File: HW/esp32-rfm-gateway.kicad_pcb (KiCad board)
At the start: 2 copper layers, 99 x 93.5 mm, 88 parts, among them J1 ph_1x2, J2 ph_1x2, J20 220V~, J21 ph_1x2, J22 s14500, J23 s18650, J24 ph_1x3, J25 ph_1x2, J3 ph_1x3, J30 AntSMA, J4 ph_1x4, J40 ph_1x2, J5 ph_1x4, J6 ph_1x3, J7 ph_1x4, J8 ph_1x6, Q20 IRLML2244, Q40 BC817, Q41 BC817, U1 ESP-WROOM-32, U2 BD48K30, U20 IRM-05, U21 MCP73832T-2ACI, U22 BD49K35, U23 TLV62569DBV, U24 TLV379IDBV, U30 RFM9x, U40 AT_CryptoAuth, U41 HDC1080DMB

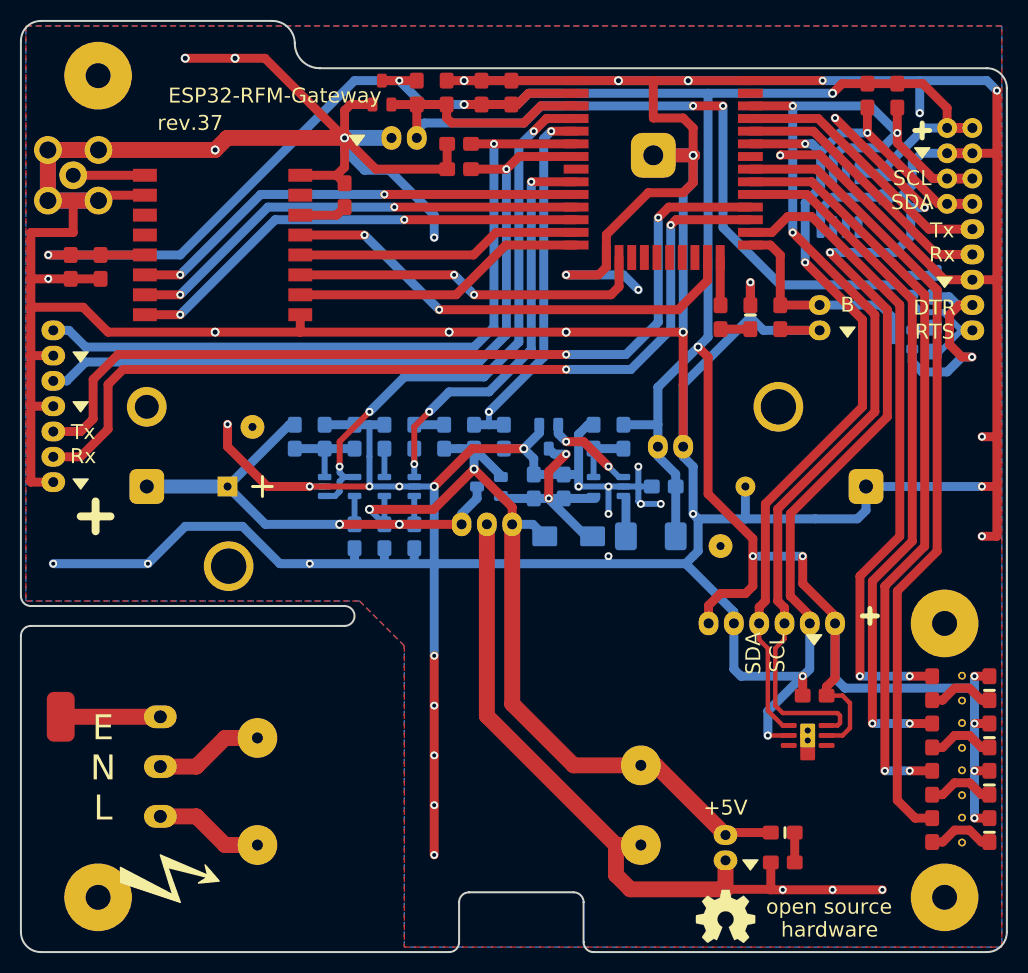
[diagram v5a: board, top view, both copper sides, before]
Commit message: Improves the labels and label positioning.
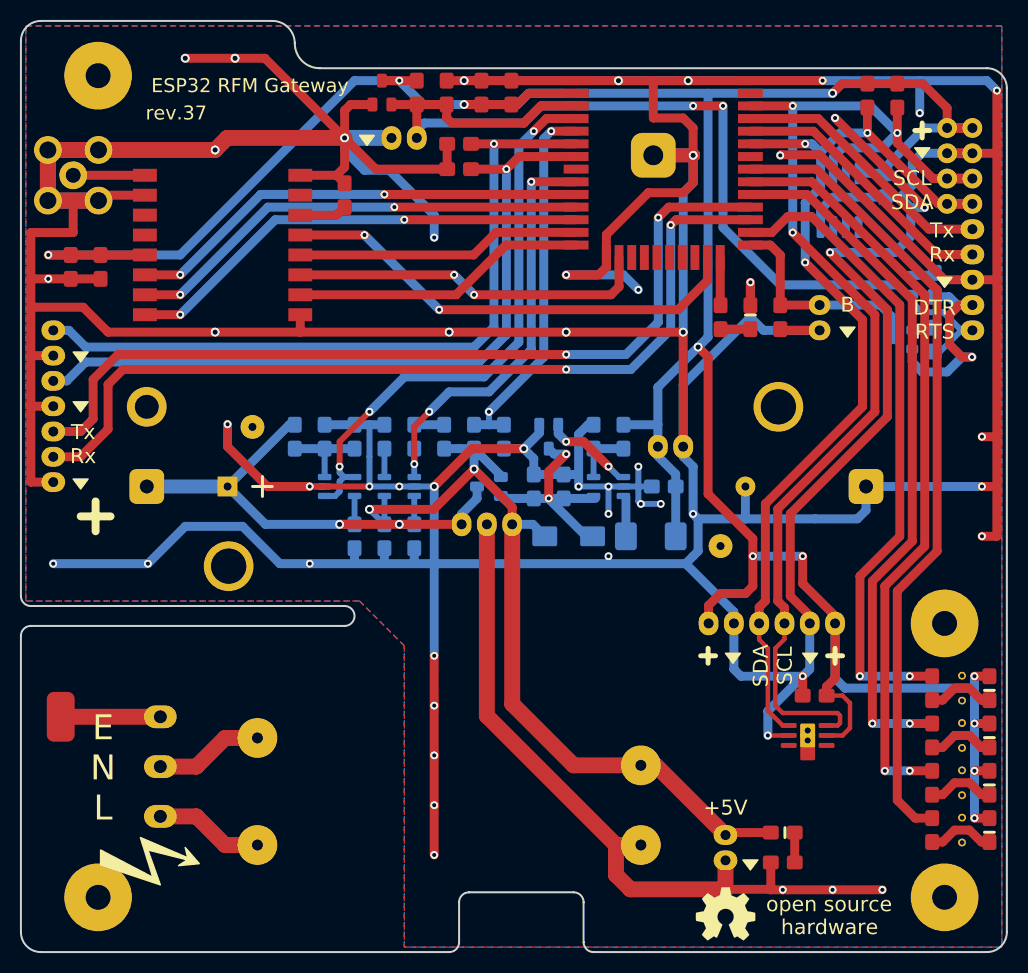
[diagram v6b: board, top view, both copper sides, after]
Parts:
- SYM5: value ESP32-RFM-Gateway -> ESP32 RFM Gateway
- moved SYM5 4.10 mm to (58.2, 53.8)
- moved SYM3 2.66 mm to (49.0, 128.2)
- moved SYM2 0.25 mm to (106.8, 133.8)
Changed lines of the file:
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@@
   (general
     (thickness 1.6)
-    (drawings 64)
+    (drawings 67)
     (tracks 745)
     (zones 0)
@@
   )
   (setup
-    (last_trace_width 0.9)
+    (last_trace_width 0.25)
     (user_trace_width 0.45)
     (user_trace_width 0.6)
@@
   )
   (module CalinGeneric:Symbol_HighVoltage_SilkS (layer F.Cu)
-    (at 51 130 90)
+    (at 49 128.25 90)
     (attr virtual)
     (fp_text reference SYM3 (at 0 -6 90) (layer F.Fab) hide
@@
   )
   (module CalinGeneric:OSHW-Logo_SilkS (layer F.Cu)
-    (at 106.75 134)
+    (at 106.75 133.75)
     (tags "Logo OSHW")
     (attr virtual)
@@
   )
   (module CalinGeneric:ValueAsText (layer F.Cu)
-    (at 61.5 51.25)
+    (at 58.25 53.75)
     (attr virtual)
     (fp_text reference SYM5 (at 0 0) (layer F.Fab) hide
       (effects (font (size 1 1) (thickness 0.15)))
     )
-    (fp_text value ESP32-RFM-Gateway (at 0 0) (layer F.SilkS)
-      (effects (font (size 1.5 1.5) (thickness 0.3)))
+    (fp_text value "ESP32 RFM Gateway" (at 0.75 -3.5) (layer F.SilkS)
+      (effects (font (size 1.4 1.4) (thickness 0.3)))
     )
     (fp_line (start -2.5 0) (end 2.5 0) (layer F.Fab) (width 0.15))
@@
       (effects (font (size 1 1) (thickness 0.15)))
     )
-    (fp_text value ph_1x6 (at 2.54 3.81) (layer F.Fab)
+    (fp_text value ph_1x6 (at -2.25 6) (layer F.Fab)
       (effects (font (size 1 1) (thickness 0.15)))
     )
@@
     )
   )
+  (gr_poly (pts (xy 106.75 107.25) (xy 108.25 107.25) (xy 107.5 108.25)) (layer F.SilkS) (width 0.15))
+  (gr_line (start 104.25 107.5) (end 105.75 107.5) (layer F.SilkS) (width 0.5))
+  (gr_line (start 105 106.75) (end 105 108.25) (layer F.SilkS) (width 0.5))
   (gr_text +5V (at 106.75 122.75) (layer F.SilkS)
     (effects (font (size 1.5 1.5) (thickness 0.3)))
   )
   (gr_poly (pts (xy 108.5 128) (xy 110 128) (xy 109.25 129)) (layer F.SilkS) (width 0.15))
-  (gr_line (start 120.5 103.5) (end 122 103.5) (layer F.SilkS) (width 0.5))
-  (gr_line (start 121.25 102.75) (end 121.25 104.25) (layer F.SilkS) (width 0.5))
-  (gr_text "SDA\nSCL" (at 110.75 107.25 90) (layer F.SilkS)
+  (gr_line (start 117 107.5) (end 118.5 107.5) (layer F.SilkS) (width 0.5))
+  (gr_line (start 117.75 106.75) (end 117.75 108.25) (layer F.SilkS) (width 0.5))
+  (gr_text "SDA\nSCL" (at 111.5 108.5 90) (layer F.SilkS)
     (effects (font (size 1.5 1.5) (thickness 0.3)))
   )
-  (gr_poly (pts (xy 114.9 105.4) (xy 116.4 105.4) (xy 115.65 106.4)) (layer F.SilkS) (width 0.15))
+  (gr_poly (pts (xy 114.5 107.25) (xy 116 107.25) (xy 115.25 108.25)) (layer F.SilkS) (width 0.15))
   (gr_line (start 126.5 54) (end 126.5 55.5) (layer F.SilkS) (width 0.5))
   (gr_line (start 125.75 54.75) (end 127.25 54.75) (layer F.SilkS) (width 0.5))
@@
   (gr_poly (pts (xy 41.25 82) (xy 42.75 82) (xy 42 83)) (layer F.SilkS) (width 0.15))
   (gr_poly (pts (xy 41.25 77) (xy 42.75 77) (xy 42 78)) (layer F.SilkS) (width 0.15))
-  (gr_poly (pts (xy 69 55.25) (xy 70.5 55.25) (xy 69.75 56.25)) (layer F.SilkS) (width 0.15))
+  (gr_poly (pts (xy 70 55.25) (xy 71.5 55.25) (xy 70.75 56.25)) (layer F.SilkS) (width 0.15))
   (gr_poly (pts (xy 118.25 74.5) (xy 119.75 74.5) (xy 119 75.5)) (layer F.SilkS) (width 0.15))
   (gr_text B (at 119 72.25) (layer F.SilkS)
     (effects (font (size 1.5 1.5) (thickness 0.3)))
   )
-  (gr_text "designed with KiCad\nfor hand soldering" (at 93.75 122.5) (layer B.SilkS)
+  (gr_text "designed with KiCad\nfor hand soldering" (at 93.5 122.5) (layer B.SilkS)
     (effects (font (size 1.5 1.5) (thickness 0.3)) (justify left mirror))
   )
-  (gr_text "github.com\n   CalinRadoni\n      esp32-rfm-gateway" (at 106.5 107.25) (layer B.SilkS)
+  (gr_text "github.com\n   CalinRadoni\n      esp32-rfm-gateway" (at 105.75 111) (layer B.SilkS)
     (effects (font (size 1.5 1.5) (thickness 0.3)) (justify left mirror))
   )
-  (gr_text rev.37 (at 53 54) (layer F.SilkS)
-    (effects (font (size 1.5 1.5) (thickness 0.3)))
+  (gr_text rev.37 (at 51.6 53) (layer F.SilkS)
+    (effects (font (size 1.4 1.4) (thickness 0.3)))
   )
   (dimension 15 (width 0.3) (layer Dwgs.User)
@@
   (gr_line (start 38 137.25) (end 79 137.25) (layer Edge.Cuts) (width 0.2))
   (gr_line (start 36 105.5) (end 36 135.25) (layer Edge.Cuts) (width 0.2))
-  (via (at 80.5 49.745) (size 0.9) (drill 0.5) (layers F.Cu B.Cu) (net 2))
-  (via (at 80.5 52.145) (size 0.9) (drill 0.5) (layers F.Cu B.Cu) (net 4) (status 1000000))
   (segment (start 56.75 90.5) (end 48.64 90.5) (width 1.4) (layer B.Cu) (net 1) (status 30))
   (via (at 68 94.3) (size 0.9) (drill 0.5) (layers F.Cu B.Cu) (net 1))
@@
   (segment (start 60.55 94.3) (end 56.75 90.5) (width 0.9) (layer B.Cu) (net 1) (status 20))
   (segment (start 68 94.3) (end 60.55 94.3) (width 0.9) (layer B.Cu) (net 1))
+  (via (at 80.5 49.745) (size 0.9) (drill 0.5) (layers F.Cu B.Cu) (net 2))
   (via (at 111 115.5) (size 0.8) (drill 0.4) (layers F.Cu B.Cu) (net 2))
   (via (at 114.5 109.55) (size 0.8) (drill 0.4) (layers F.Cu B.Cu) (net 2))
@@
   (segment (start 75.75 54.75) (end 75.75 55.5) (width 0.9) (layer B.Cu) (net 3))
   (segment (start 76.5 54) (end 75.75 54.75) (width 0.9) (layer B.Cu) (net 3))
+  (via (at 80.5 52.145) (size 0.9) (drill 0.5) (layers F.Cu B.Cu) (net 4))
   (via (at 104 76.5) (size 0.9) (drill 0.5) (layers F.Cu B.Cu) (net 4))
   (via (at 38.75 67.25) (size 0.8) (drill 0.4) (layers F.Cu B.Cu) (net 4))

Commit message: Adds a capacitor for humidity sensor, extended I2C socket or LEDs.
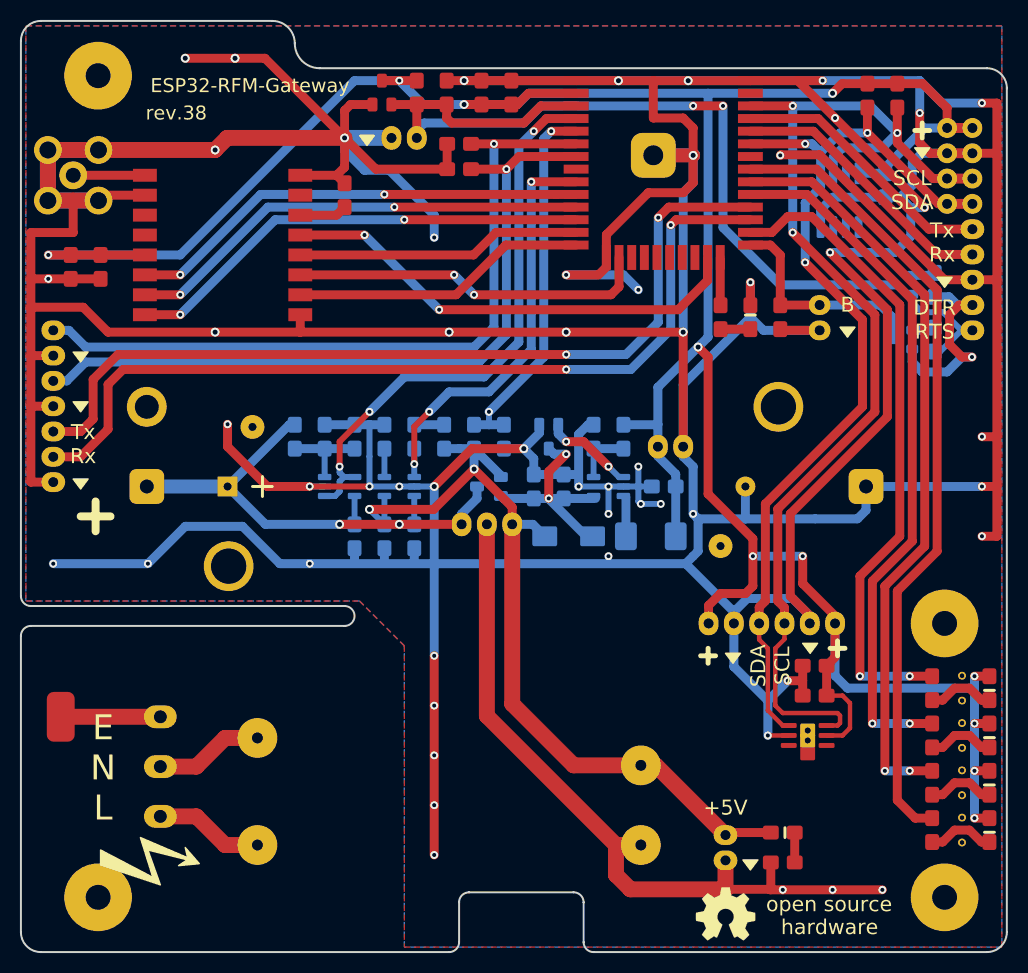
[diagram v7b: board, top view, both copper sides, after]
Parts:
- added C10: 10uF, CalinGeneric:C0805HS, F.Cu at (115.7, 108.5)
- SYM5: value ESP32 RFM Gateway -> ESP32-RFM-Gateway
- moved C31 3.00 mm to (41.0, 68.5)
- moved C32 3.00 mm to (44.0, 68.5)
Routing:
- net GND: track 977.8 -> 994.0 mm
- net /SDA: track 95.4 -> 97.9 mm
- net /SCL: track 115.0 -> 117.5 mm
- net +3V3: track 293.8 -> 296.2 mm
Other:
- board text added: "rev.38"
- board text removed: "rev.37"

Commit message: Creates the files for PCB fabrication, and adjusts the PCB layout a little.
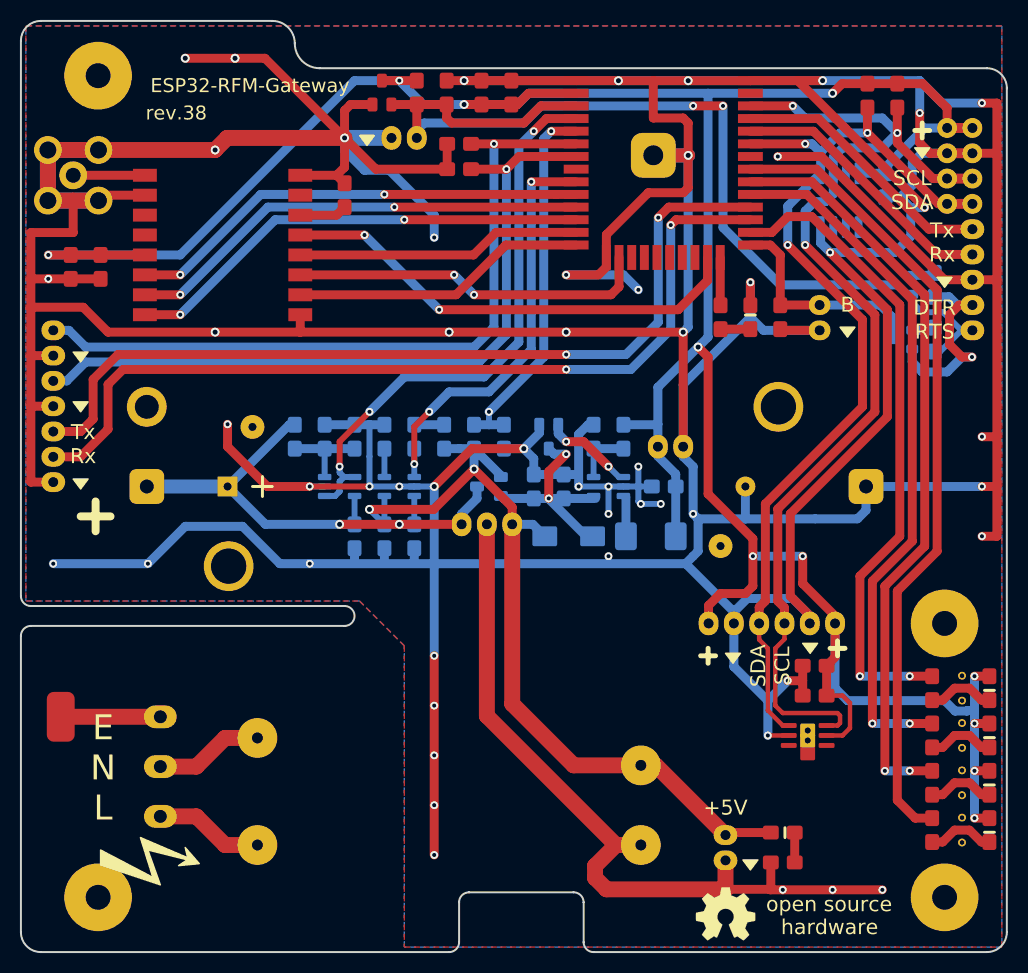
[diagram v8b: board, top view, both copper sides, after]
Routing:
- net /SCL: track 117.5 -> 112.0 mm
- net GND: track 994.0 -> 989.8 mm, vias 54 -> 53
- net +3V3: track 296.2 -> 297.9 mm
- net /SDA: track 97.9 -> 99.4 mm
